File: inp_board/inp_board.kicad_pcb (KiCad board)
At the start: 2 copper layers, 2 parts

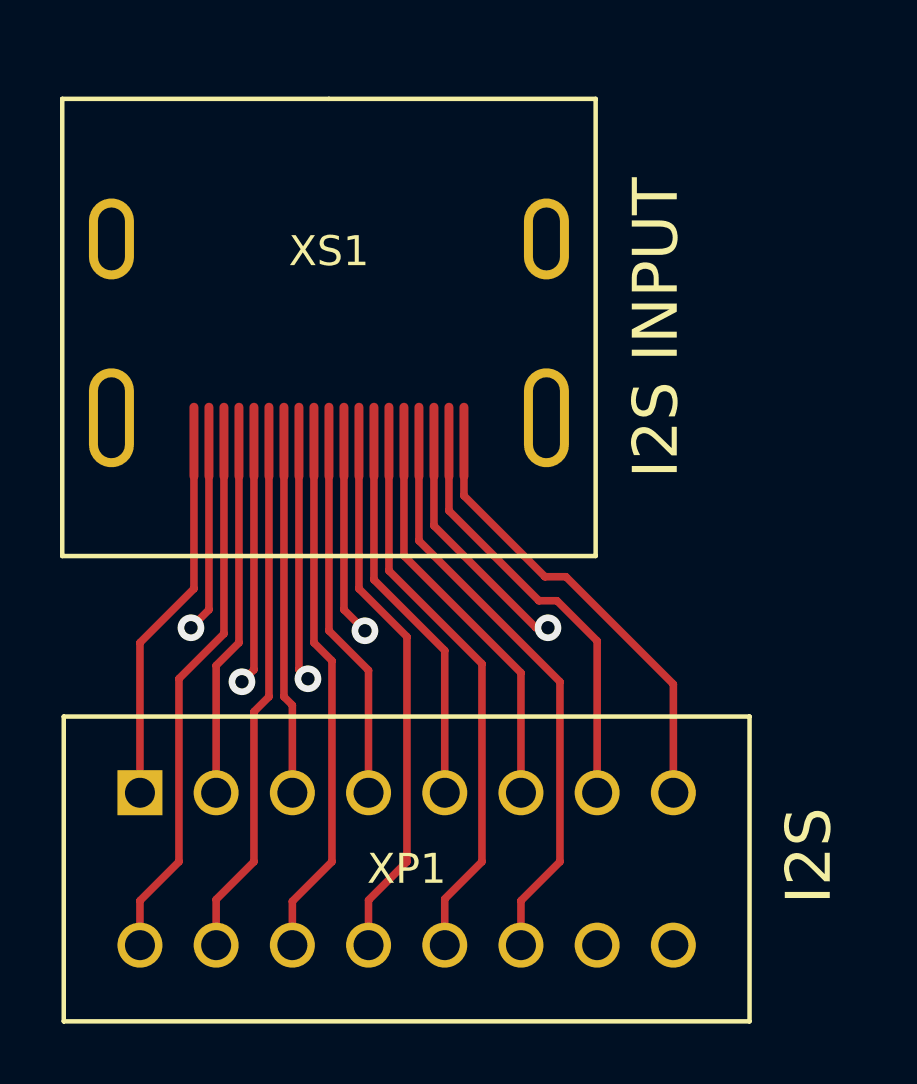
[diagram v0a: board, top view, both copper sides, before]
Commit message: spdif part added
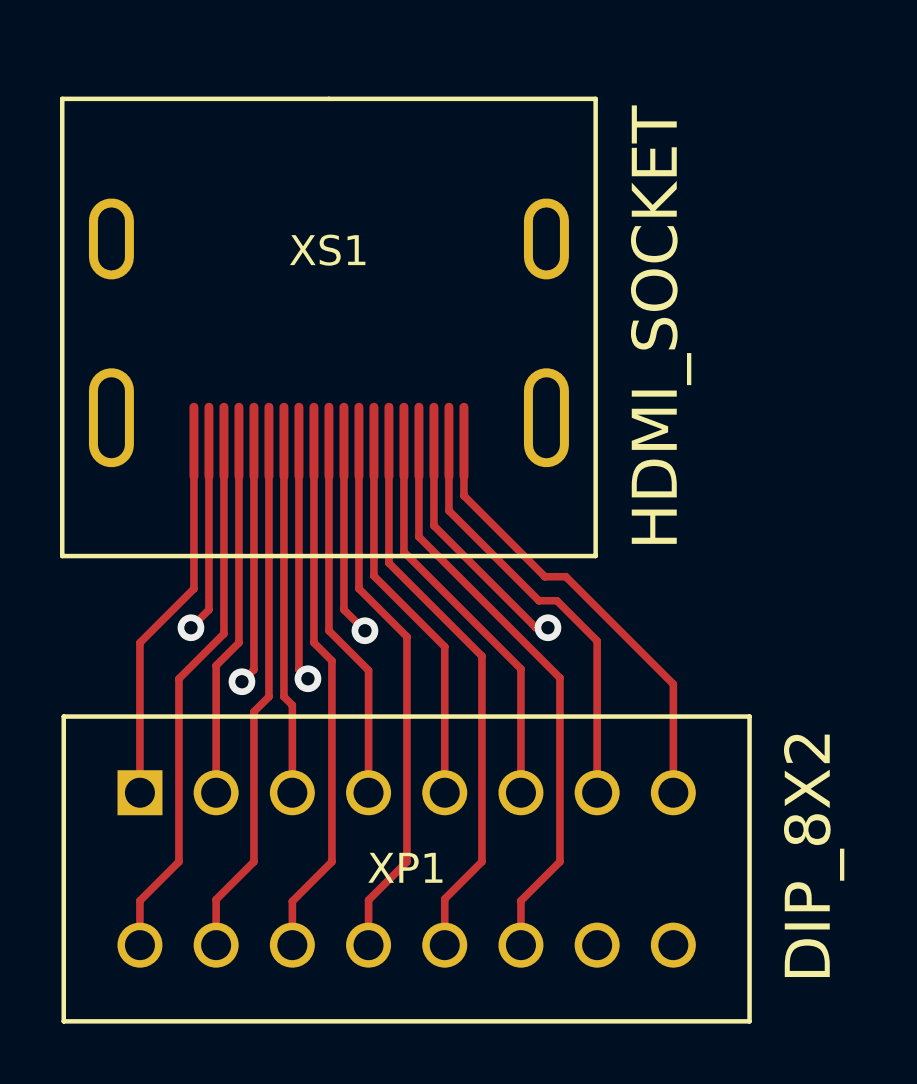
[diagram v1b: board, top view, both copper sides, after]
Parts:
- XP1: value I2S -> DIP_8X2
- XS1: value I2S INPUT -> HDMI_SOCKET
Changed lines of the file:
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@@
-(kicad_pcb (version 3) (host pcbnew "(2013-june-11)-stable")
+(kicad_pcb (version 3) (host pcbnew "(2013-07-07 BZR 4022)-stable")
   (general
     (links 24)
     (no_connects 10)
-    (area 77.089 73.279 126.111 96.901)
+    (area 0 0 0 0)
     (thickness 1.6)
     (drawings 0)
@@
     (pad_to_mask_clearance 0)
     (aux_axis_origin 0 0)
-    (visible_elements FFFFFFBF)
+    (visible_elements 7FFFFFFF)
     (pcbplotparams
       (layerselection 3178497)
@@
       (effects (font (size 1 1) (thickness 0.15)))
     )
-    (fp_text value "I2S INPUT" (at -10.9 3.8 270) (layer F.SilkS)
+    (fp_text value HDMI_SOCKET (at -10.9 3.8 270) (layer F.SilkS)
       (effects (font (size 1.5 1.5) (thickness 0.2)))
     )
@@
       (effects (font (size 1 1) (thickness 0.15)))
     )
-    (fp_text value I2S (at 22.3 2.1 90) (layer F.SilkS)
+    (fp_text value DIP_8X2 (at 22.3 2.1 90) (layer F.SilkS)
       (effects (font (size 1.5 1.5) (thickness 0.2)))
     )
@@
   (segment (start 222.85 64.65) (end 222.85 70.75) (width 0.254) (layer F.Cu) (net 3))
   (segment (start 224.35 63.15) (end 222.85 64.65) (width 0.254) (layer F.Cu) (net 3))
-  (segment (start 229.35 56.75) (end 229.35 61.35) (width 0.254) (layer F.Cu) (net 4))
-  (segment (start 231.71 63.71) (end 231.71 68.45) (width 0.254) (layer F.Cu) (net 4))
-  (segment (start 229.35 61.35) (end 231.71 63.71) (width 0.254) (layer F.Cu) (net 4))
+  (segment (start 229.35 56.75) (end 229.35 61.223) (width 0.254) (layer F.Cu) (net 4))
+  (segment (start 231.71 63.583) (end 231.71 68.45) (width 0.254) (layer F.Cu) (net 4))
+  (segment (start 229.35 61.223) (end 231.71 63.583) (width 0.254) (layer F.Cu) (net 4))
   (segment (start 223.85 56.75) (end 223.85 62.35) (width 0.254) (layer F.Cu) (net 5))
   (via (at 223.25 62.95) (size 0.889) (layers F.Cu B.Cu) (net 5))
@@
   (segment (start 230.45 63.25) (end 230.45 70.75) (width 0.254) (layer F.Cu) (net 10))
   (segment (start 228.85 61.65) (end 230.45 63.25) (width 0.254) (layer F.Cu) (net 10))
-  (segment (start 229.85 56.75) (end 229.85 61.05) (width 0.254) (layer F.Cu) (net 11))
+  (segment (start 229.85 56.75) (end 229.85 60.796) (width 0.254) (layer F.Cu) (net 11))
   (segment (start 231.71 71.99) (end 231.71 73.53) (width 0.254) (layer F.Cu) (net 11))
   (segment (start 232.95 70.75) (end 231.71 71.99) (width 0.254) (layer F.Cu) (net 11))
-  (segment (start 232.95 64.15) (end 232.95 70.75) (width 0.254) (layer F.Cu) (net 11))
-  (segment (start 229.85 61.05) (end 232.95 64.15) (width 0.254) (layer F.Cu) (net 11))
-  (segment (start 230.35 56.75) (end 230.35 60.55) (width 0.254) (layer F.Cu) (net 12))
-  (segment (start 234.25 64.45) (end 234.25 68.45) (width 0.254) (layer F.Cu) (net 12))
-  (segment (start 230.35 60.55) (end 234.25 64.45) (width 0.254) (layer F.Cu) (net 12))
-  (segment (start 230.85 56.75) (end 230.85 60.05) (width 0.254) (layer F.Cu) (net 13))
+  (segment (start 232.95 63.896) (end 232.95 70.75) (width 0.254) (layer F.Cu) (net 11))
+  (segment (start 229.85 60.796) (end 232.95 63.896) (width 0.254) (layer F.Cu) (net 11))
+  (segment (start 230.35 56.75) (end 230.35 60.423) (width 0.254) (layer F.Cu) (net 12))
+  (segment (start 234.25 64.323) (end 234.25 68.45) (width 0.254) (layer F.Cu) (net 12))
+  (segment (start 230.35 60.423) (end 234.25 64.323) (width 0.254) (layer F.Cu) (net 12))
+  (segment (start 230.85 56.75) (end 230.85 59.923) (width 0.254) (layer F.Cu) (net 13))
   (segment (start 234.25 72.05) (end 234.25 73.53) (width 0.254) (layer F.Cu) (net 13))
   (segment (start 235.55 70.75) (end 234.25 72.05) (width 0.254) (layer F.Cu) (net 13))
-  (segment (start 235.55 64.75) (end 235.55 70.75) (width 0.254) (layer F.Cu) (net 13))
-  (segment (start 230.85 60.05) (end 235.55 64.75) (width 0.254) (layer F.Cu) (net 13))
+  (segment (start 235.55 64.623) (end 235.55 70.75) (width 0.254) (layer F.Cu) (net 13))
+  (segment (start 230.85 59.923) (end 235.55 64.623) (width 0.254) (layer F.Cu) (net 13))
   (segment (start 224.85 56.75) (end 224.85 63.45) (width 0.254) (layer F.Cu) (net 14))
   (segment (start 224.09 64.21) (end 224.09 68.45) (width 0.254) (layer F.Cu) (net 14))
